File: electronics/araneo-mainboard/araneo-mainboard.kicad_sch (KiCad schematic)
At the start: 79 parts, among them IC1 TPS54302DDCR, J1 GPIO2, J2 OLED, J3 GPIO1, SW2 SW, SW3 SW, U4 POWER, U5 PAM8403D

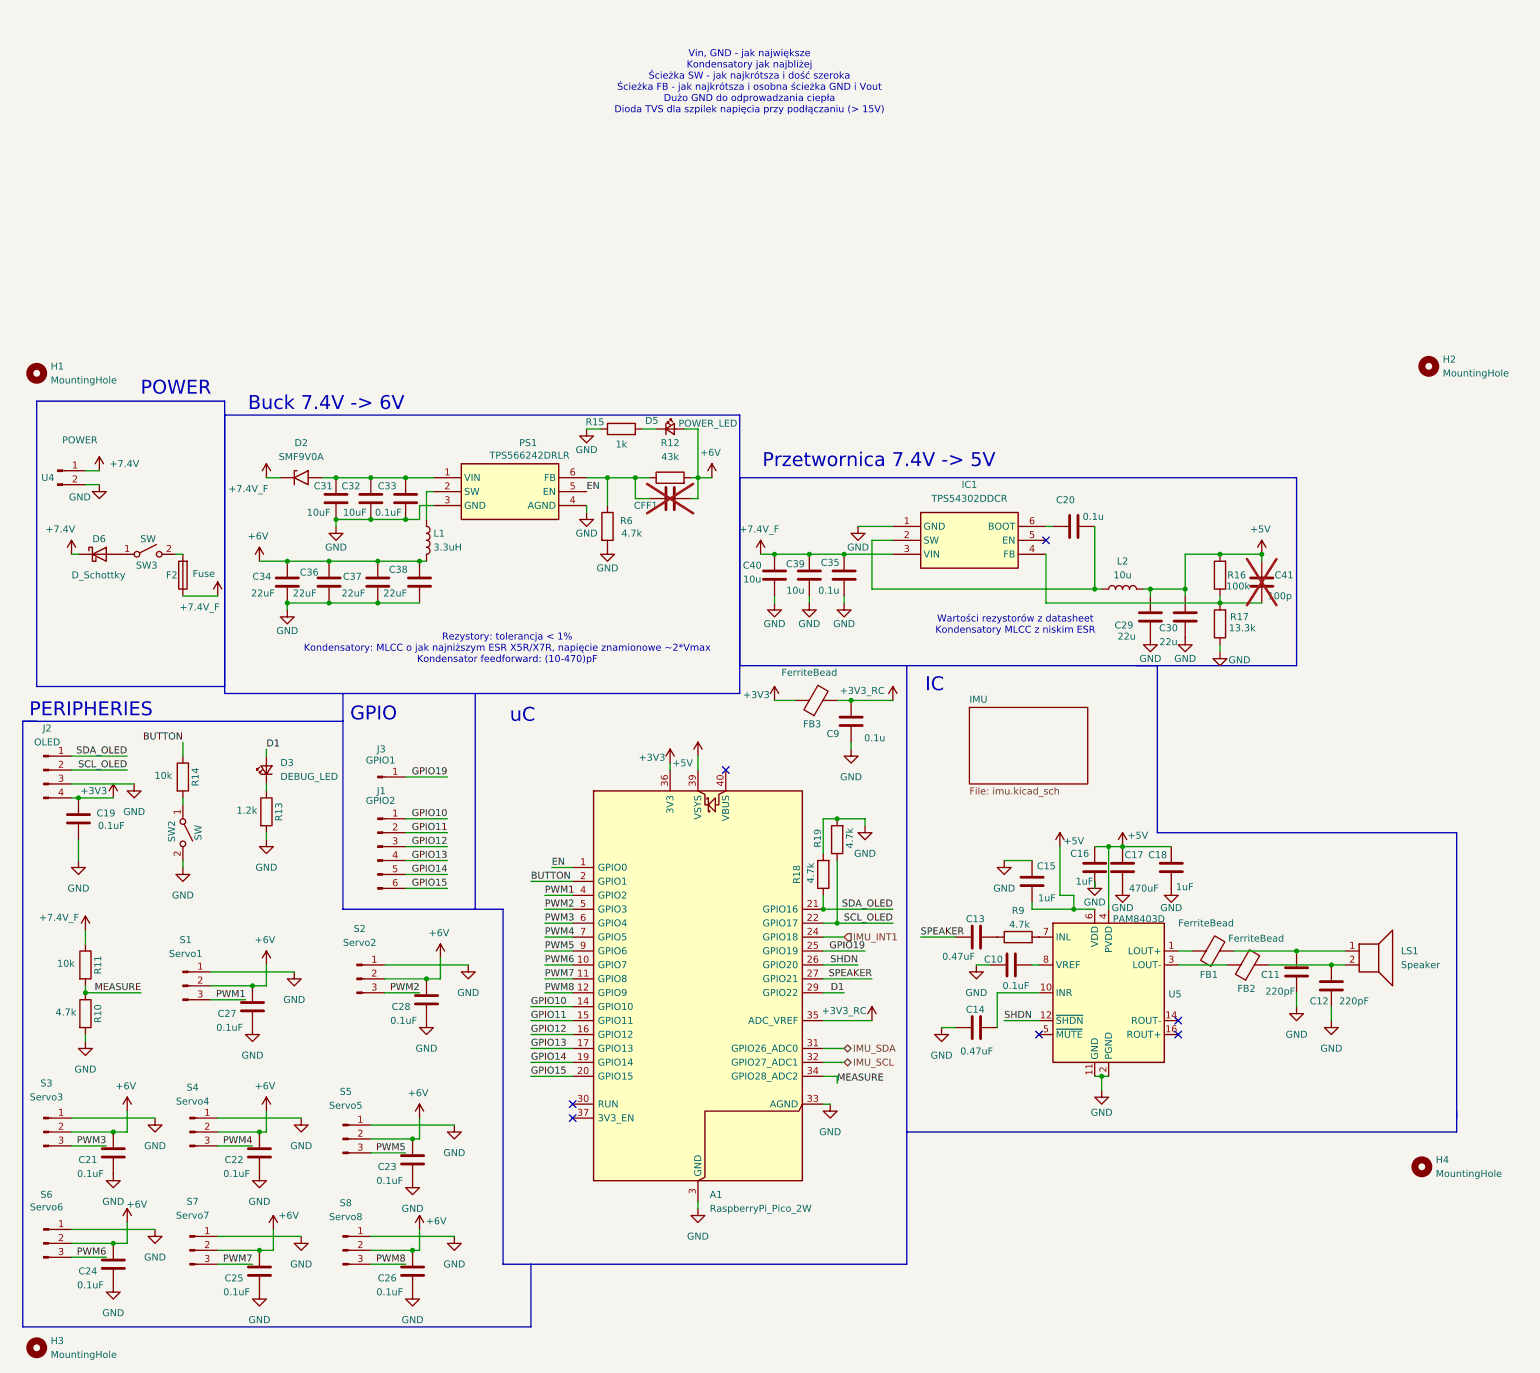
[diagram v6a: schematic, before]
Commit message: electronics: add magnetometer
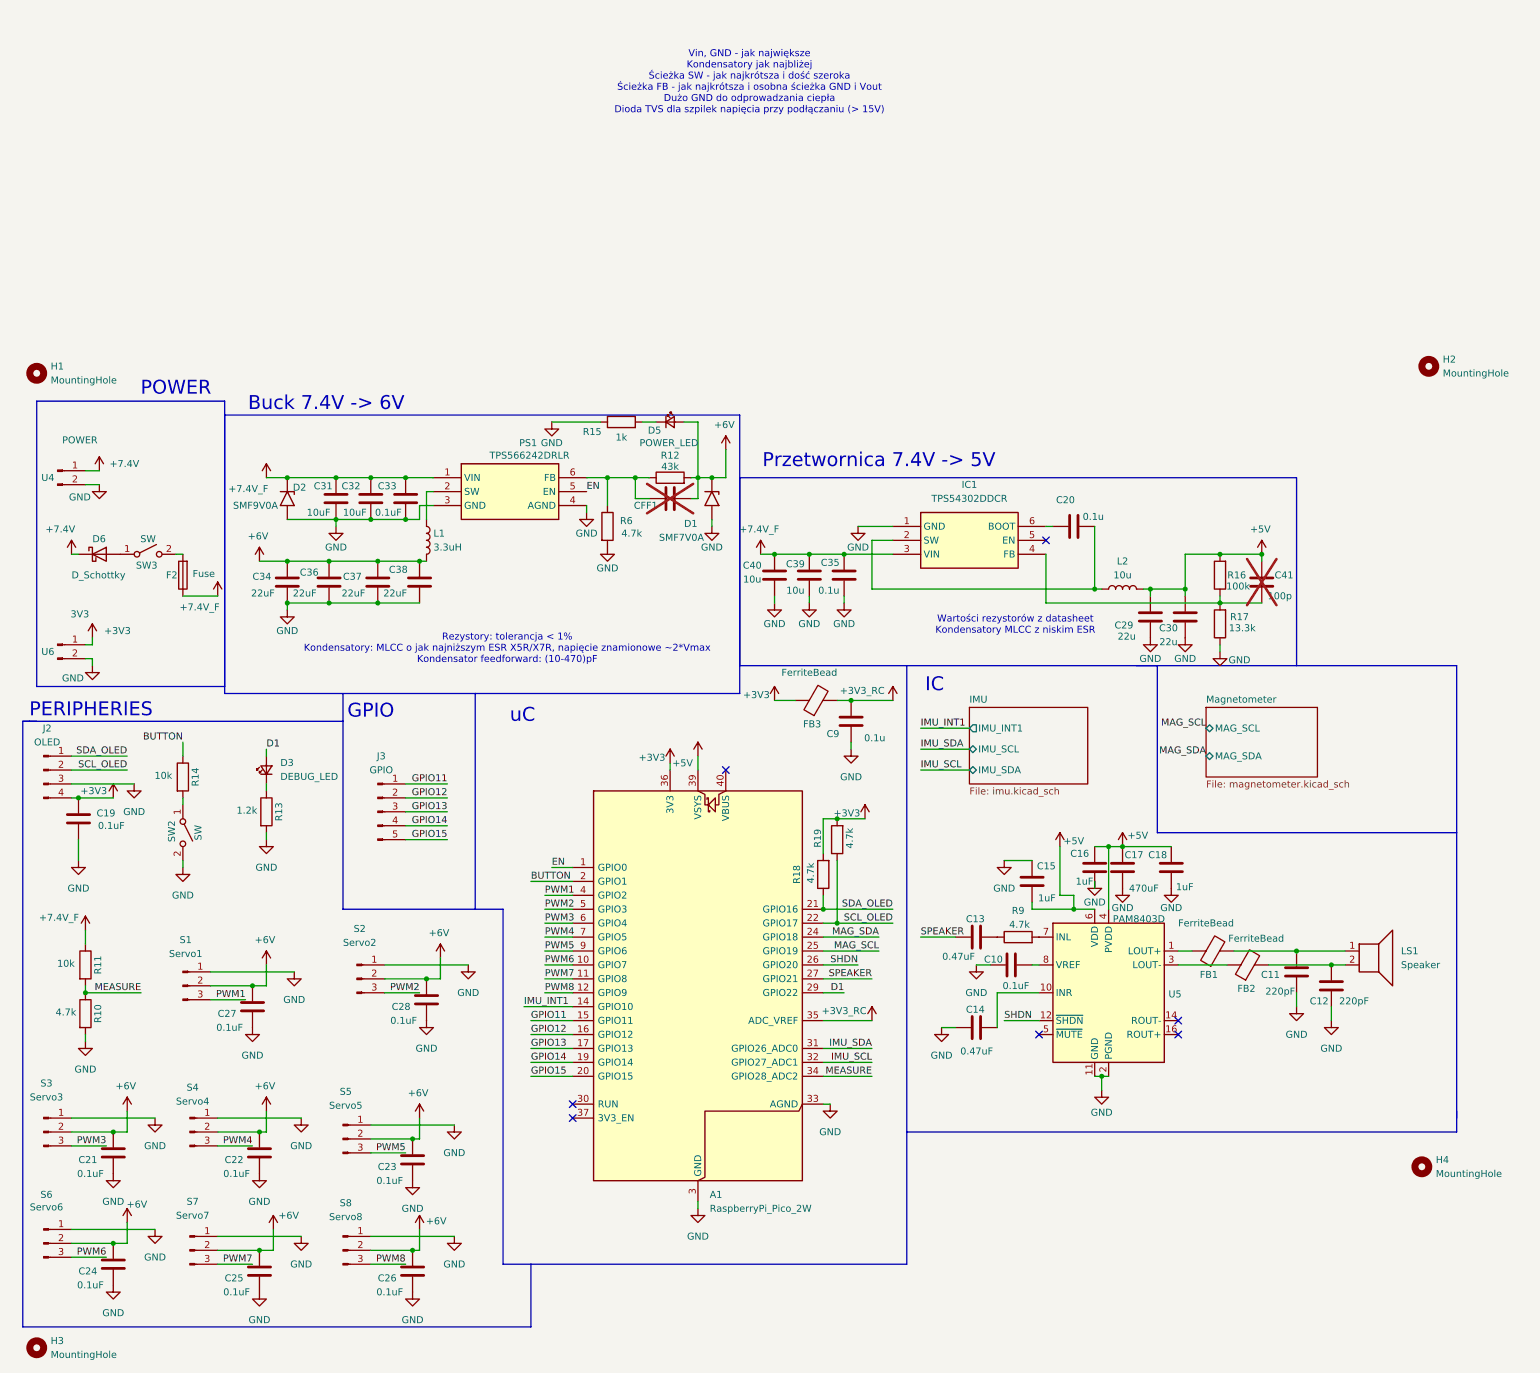
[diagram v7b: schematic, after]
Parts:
- removed J1: GPIO2, Connector_PinHeader_2.54mm:PinHeader_1x06_P2.54mm_Vertical, symbol Connector:Conn_01x06_Pin
- removed J3: GPIO1, Connector_PinHeader_2.54mm:PinHeader_1x01_P2.54mm_Vertical, symbol Connector:Conn_01x01_Pin
- added D1: SMF7V0A, Diode_SMD:D_SOD-123, symbol Diode:SMF7V0A
- added J3: GPIO, Connector_PinHeader_2.54mm:PinHeader_1x05_P2.54mm_Vertical, symbol Connector:Conn_01x05_Pin
- added U6: 3V3, Connector_PinHeader_2.54mm:PinHeader_1x02_P2.54mm_Vertical, symbol Connector:Conn_01x02_Pin
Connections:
- net GPIO10 is gone; now on net IMU_INT1: A1.14 (GPIO10)
- net +3V3: now also R18.2, R19.2, U6.1 (Pin_1)
- net +6V: now also D1.1 (A1)
- net +7.4V_F: now also C31.1, C32.1, C33.1, PS1.1 (VIN)
- net GND: now also D2.2 (A2), D1.2 (A2), U6.2 (Pin_2); no longer R18.2, R19.2
- net GPIO11: now also J3.1 (Pin_1)
- net GPIO12: now also J3.2 (Pin_2)
- net GPIO13: now also J3.3 (Pin_3)
- net GPIO14: now also J3.4 (Pin_4)
- net GPIO15: now also J3.5 (Pin_5)
- net IMU_INT1: no longer A1.24 (GPIO18)
- net GPIO19 renamed MAG_SCL
- new net MAG_SDA: A1.24 (GPIO18)
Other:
- added sheet Magnetometer (magnetometer.kicad_sch)
- sheet IMU ports: added IMU_INT1, IMU_SCL, IMU_SDA; removed none
- moved on the sheet: D5, R15

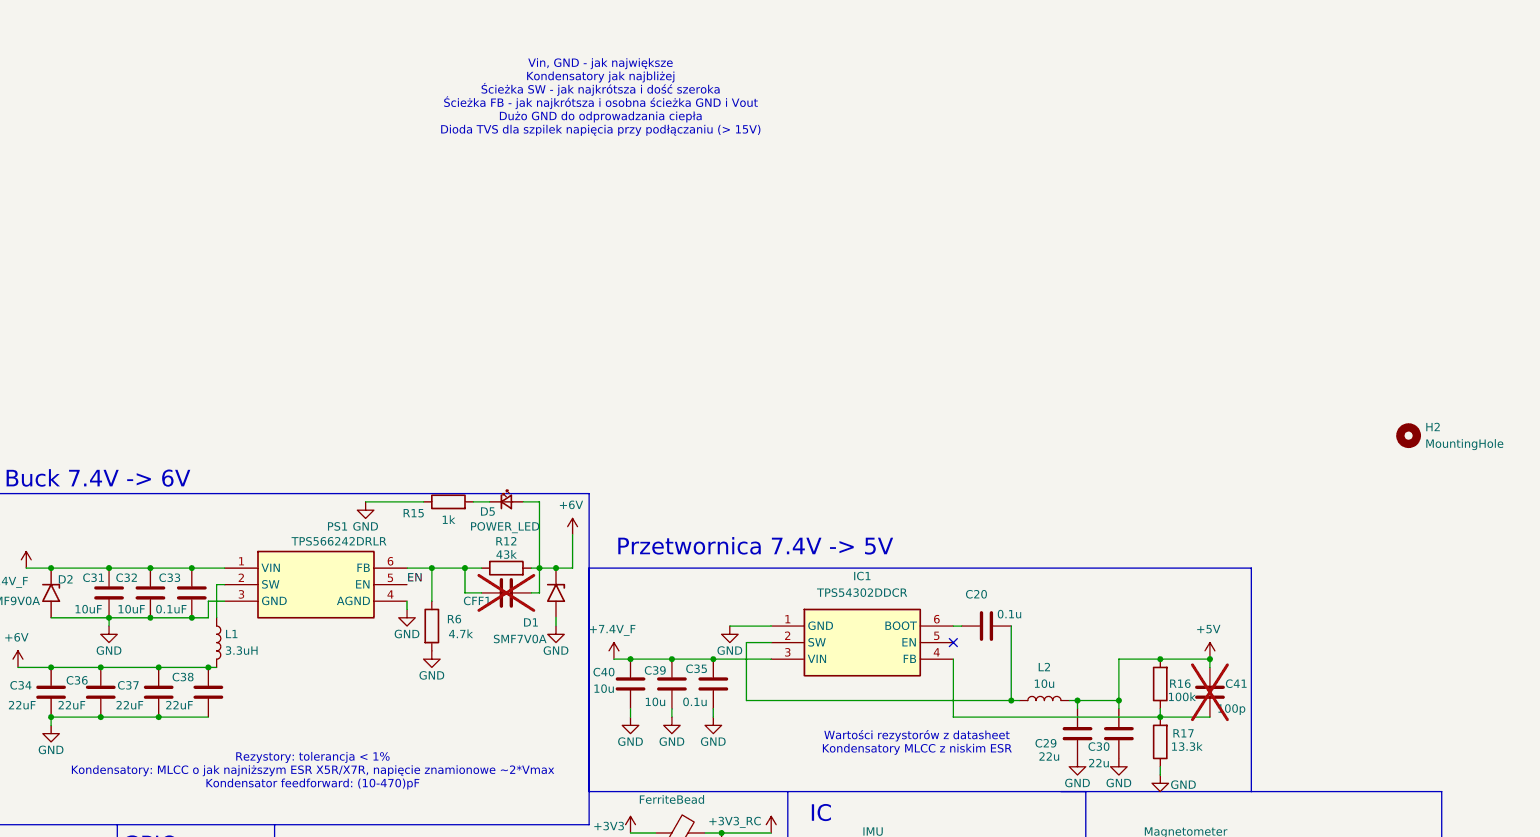
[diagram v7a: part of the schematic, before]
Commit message: electronics: add 100n capacitors
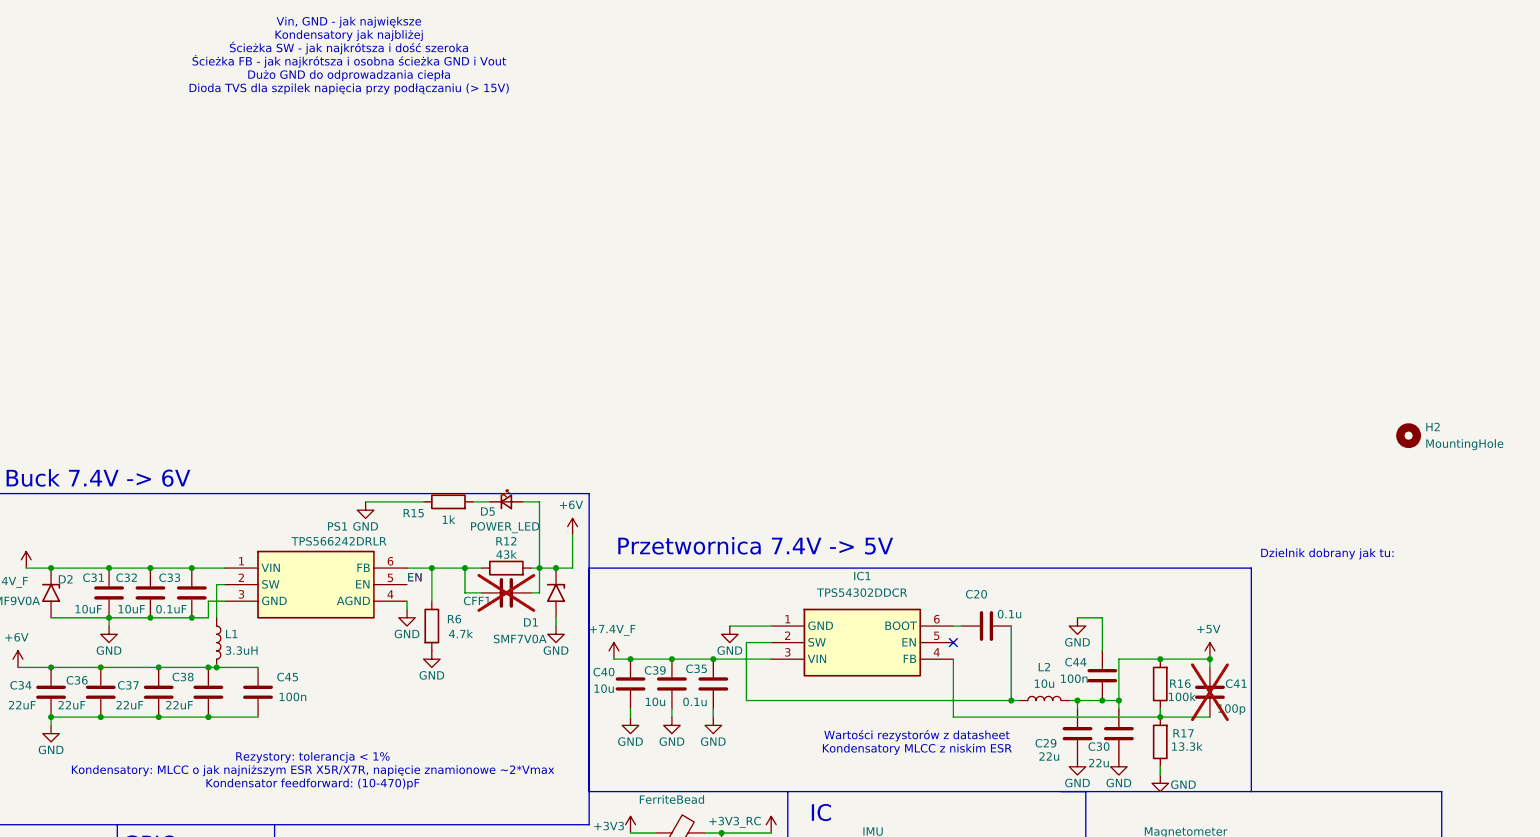
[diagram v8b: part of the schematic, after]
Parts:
- added C44, C45: 100n, Capacitor_SMD:C_0603_1608Metric_Pad1.08x0.95mm_HandSolder, symbol Device:C
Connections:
- net +5V: now also C44.2
- net +6V: now also C45.1
- net GND: now also C44.1, C45.2
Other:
- note added: "Dzielnik dobrany jak tu:"
